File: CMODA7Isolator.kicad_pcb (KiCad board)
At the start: 2 copper layers, 78.7 x 82.6 mm, 49 parts, among them J1 Conn_01x24, J2 Conn_01x24, M1 Artix_7_35T_CMOD_A7, U1 TXB0108, U2 TXB0108, U3 TXB0108, U4 TXB0108, U5 TXB0108, U6 TXB0108, U7 LD1117S33TR_SOT223

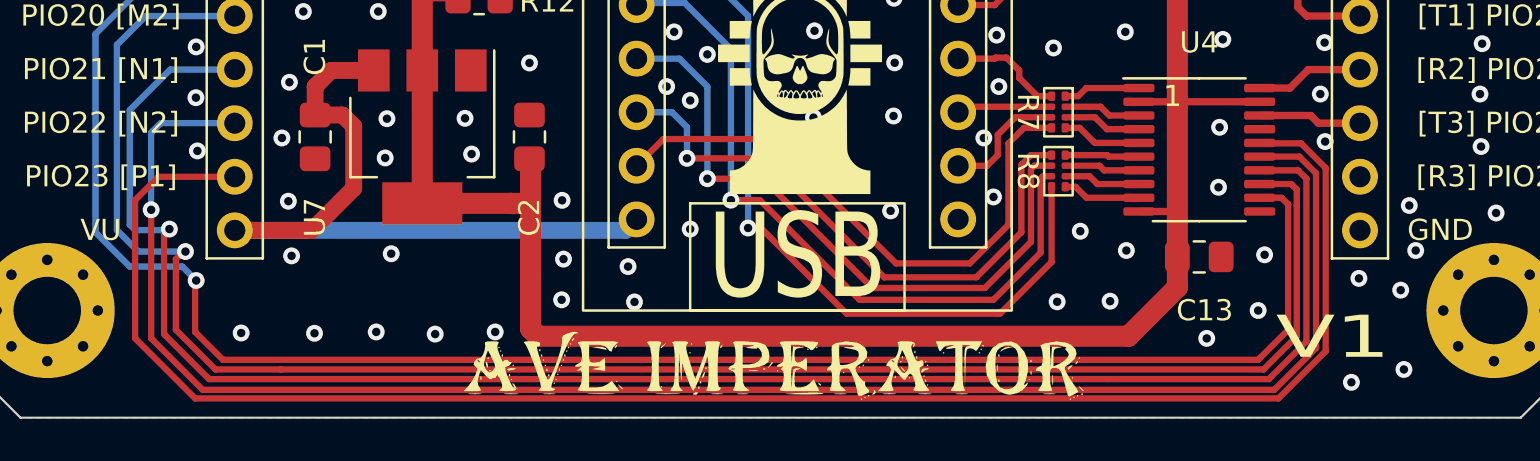
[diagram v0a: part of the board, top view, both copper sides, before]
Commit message: Fixed Issue #3
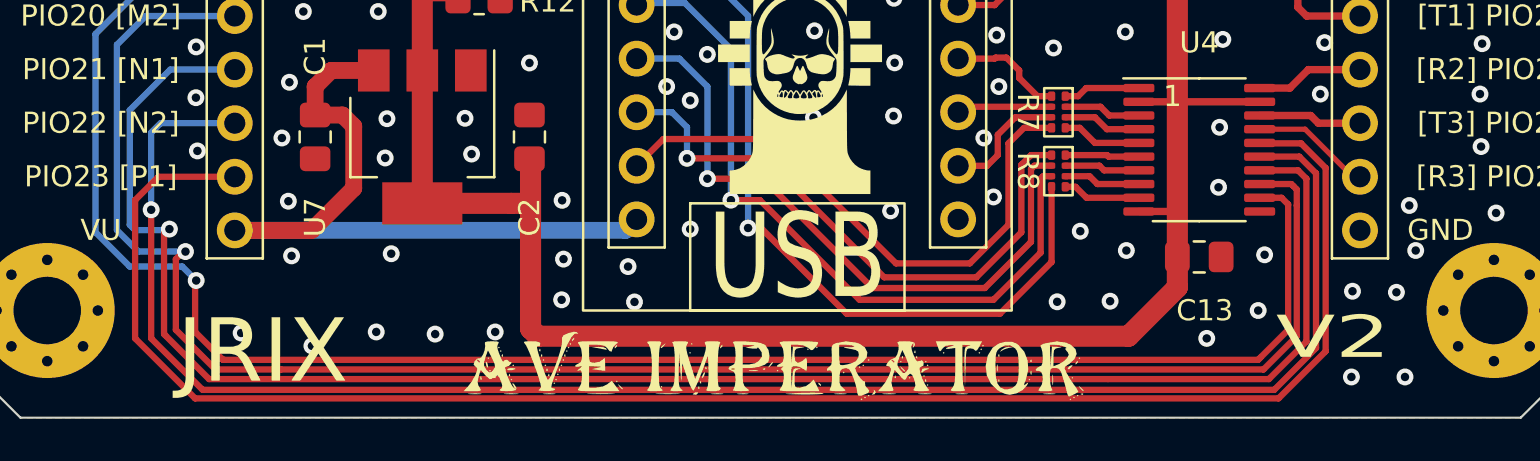
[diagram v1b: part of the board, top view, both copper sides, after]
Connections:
- U4 pad 17: /p024 -> /p026
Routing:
- net /p026: track 0.00 -> 5.69 mm
- net GND: vias 277 -> 276
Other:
- board text added: "JRIX"
- board text added: "V2"
- board text removed: "V1"
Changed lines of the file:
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@@
   (net 136 "/p39")
   (net 137 "/p40")
-  (net 138 "/p024")
+  (net 138 "Net-(D5-Pad2)")
   (net 139 "unconnected-(U6-Pad1)")
   (net 140 "unconnected-(U6-Pad3)")
@@
   (net 145 "unconnected-(U6-Pad18)")
   (net 146 "unconnected-(U6-Pad20)")
-  (net 147 "Net-(R12-Pad2)")
   (footprint "MountingHole:MountingHole_3.2mm_M3_Pad_Via" (layer "F.Cu")
     (at 53.34 39.37)
@@
       (net 2 "GND") (pinfunction "K") (pintype "passive"))
     (pad "2" smd roundrect (at 0.7875 0 293) (size 0.875 0.95) (layers "F.Cu" "F.Paste" "F.Mask") (roundrect_rratio 0.25)
-      (net 147 "Net-(R12-Pad2)") (pinfunction "A") (pintype "passive"))
+      (net 138 "Net-(D5-Pad2)") (pinfunction "A") (pintype "passive"))
     (model "${KICAD6_3DMODEL_DIR}/LED_SMD.3dshapes/LED_0603_1608Metric.wrl"
       (offset (xyz 0 0 0))
@@
       (net 3 "/3V3") (pintype "passive"))
     (pad "2" smd roundrect (at 1 0) (size 1.2 1.4) (layers "F.Cu" "F.Paste" "F.Mask") (roundrect_rratio 0.2083333333)
-      (net 147 "Net-(R12-Pad2)") (pintype "passive"))
+      (net 138 "Net-(D5-Pad2)") (pintype "passive"))
     (model "${KICAD6_3DMODEL_DIR}/Resistor_SMD.3dshapes/R_0805_2012Metric.wrl"
       (offset (xyz 0 0 0))
@@
       (net 26 "/p023") (pinfunction "B4") (pintype "bidirectional"))
     (pad "17" smd roundrect (at 2.8625 -0.975) (size 1.475 0.4) (layers "F.Cu" "F.Paste" "F.Mask") (roundrect_rratio 0.25)
-      (net 138 "/p024") (pinfunction "B3") (pintype "bidirectional"))
+      (net 49 "/p026") (pinfunction "B3") (pintype "bidirectional"))
     (pad "18" smd roundrect (at 2.8625 -1.625) (size 1.475 0.4) (layers "F.Cu" "F.Paste" "F.Mask") (roundrect_rratio 0.25)
       (net 48 "/p027") (pinfunction "B2") (pintype "bidirectional"))
@@
     (effects (font (size 1 1) (thickness 0.15)))
   )
-  (gr_text "V1" (at 114.3 113.03) (layer "F.SilkS")
+  (gr_text "V2" (at 114.3 113.03) (layer "F.SilkS")
     (effects (font (size 2 3) (thickness 0.5)))
   )
@@
     (effects (font (size 1 1) (thickness 0.15)))
   )
+  (gr_text "JRIX" (at 63.5508 113.6904) (layer "F.SilkS")
+    (effects (font (size 3 3) (thickness 0.4)))
+  )
   (gr_text "PIO19 [P3]" (at 55.88 95.25) (layer "F.SilkS")
     (effects (font (size 1 1) (thickness 0.15)))
@@
   (via (at 74.5744 112.776) (size 0.8) (drill 0.4) (layers "F.Cu" "B.Cu") (net 2))
   (via (at 64.9224 109.1692) (size 0.8) (drill 0.4) (layers "F.Cu" "B.Cu") (net 2))
-  (via (at 115.1636 115.1636) (size 0.8) (drill 0.4) (layers "F.Cu" "B.Cu") (net 2))
+  (via (at 115.1636 114.9096) (size 0.8) (drill 0.4) (layers "F.Cu" "B.Cu") (net 2))
   (via (at 93.458674 102.538985) (size 0.8) (drill 0.4) (layers "F.Cu" "B.Cu") (net 2))
   (via (at 93.6244 65.1764) (size 0.8) (drill 0.4) (layers "F.Cu" "B.Cu") (net 2))
@@
   (via (at 87.376 37.9476) (size 0.8) (drill 0.4) (layers "F.Cu" "B.Cu") (net 2))
   (via (at 80.2132 60.452) (size 0.8) (drill 0.4) (layers "F.Cu" "B.Cu") (net 2))
-  (via (at 113.917987 103.751487) (size 0.8) (drill 0.4) (layers "F.Cu" "B.Cu") (net 2))
   (via (at 63.754 78.5876) (size 0.8) (drill 0.4) (layers "F.Cu" "B.Cu") (net 2))
   (via (at 93.440454 91.123201) (size 0.8) (drill 0.4) (layers "F.Cu" "B.Cu") (net 2))
@@
   (via (at 97.7392 85.9028) (size 0.8) (drill 0.4) (layers "F.Cu" "B.Cu") (net 2))
   (via (at 73.4568 104.3432) (size 0.8) (drill 0.4) (layers "F.Cu" "B.Cu") (net 2))
-  (via (at 66.009829 112.839191) (size 0.8) (drill 0.4) (layers "F.Cu" "B.Cu") (net 2))
+  (via (at 65.8876 113.4364) (size 0.8) (drill 0.4) (layers "F.Cu" "B.Cu") (net 2))
   (via (at 89.027 91.313) (size 0.8) (drill 0.4) (layers "F.Cu" "B.Cu") (net 2))
   (via (at 50.209422 49.290135) (size 0.8) (drill 0.4) (layers "F.Cu" "B.Cu") (net 2))
@@
   (via (at 58.61089 40.806027) (size 0.8) (drill 0.4) (layers "F.Cu" "B.Cu") (net 2))
   (via (at 94.1324 40.5892) (size 0.8) (drill 0.4) (layers "F.Cu" "B.Cu") (net 2))
-  (via (at 117.6528 114.554) (size 0.8) (drill 0.4) (layers "F.Cu" "B.Cu") (net 2))
+  (via (at 117.7036 114.9096) (size 0.8) (drill 0.4) (layers "F.Cu" "B.Cu") (net 2))
   (via (at 68.9356 112.776) (size 0.8) (drill 0.4) (layers "F.Cu" "B.Cu") (net 2))
   (via (at 110.8456 63.3476) (size 0.8) (drill 0.4) (layers "F.Cu" "B.Cu") (net 2))
@@
   (via (at 97.8916 90.6272) (size 0.8) (drill 0.4) (layers "F.Cu" "B.Cu") (net 2))
   (via (at 50.114783 54.447968) (size 0.8) (drill 0.4) (layers "F.Cu" "B.Cu") (net 2))
-  (via (at 115.5192 110.236) (size 0.8) (drill 0.4) (layers "F.Cu" "B.Cu") (net 2))
+  (via (at 115.2144 110.8456) (size 0.8) (drill 0.4) (layers "F.Cu" "B.Cu") (net 2))
   (via (at 107.7976 47.3456) (size 0.8) (drill 0.4) (layers "F.Cu" "B.Cu") (net 2))
   (via (at 98.163883 52.776328) (size 0.8) (drill 0.4) (layers "F.Cu" "B.Cu") (net 2))
@@
   (via (at 93.493622 76.867361) (size 0.8) (drill 0.4) (layers "F.Cu" "B.Cu") (net 2))
   (via (at 50.256742 80.994248) (size 0.8) (drill 0.4) (layers "F.Cu" "B.Cu") (net 2))
-  (via (at 117.5004 110.7948) (size 0.8) (drill 0.4) (layers "F.Cu" "B.Cu") (net 2))
+  (via (at 117.2972 110.8964) (size 0.8) (drill 0.4) (layers "F.Cu" "B.Cu") (net 2))
   (via (at 98.3488 88.4936) (size 0.8) (drill 0.4) (layers "F.Cu" "B.Cu") (net 2))
   (via (at 84.0232 67.9196) (size 0.8) (drill 0.4) (layers "F.Cu" "B.Cu") (net 2))
@@
   (segment (start 113.2338 102.515) (end 113.5988 102.88) (width 0.35) (layer "F.Cu") (net 48))
   (segment (start 110.8125 102.515) (end 113.2338 102.515) (width 0.35) (layer "F.Cu") (net 48))
+  (segment (start 112.9694 103.165) (end 115.2244 105.42) (width 0.25) (layer "F.Cu") (net 49))
+  (segment (start 110.8125 103.165) (end 112.9694 103.165) (width 0.25) (layer "F.Cu") (net 49))
+  (segment (start 115.2244 105.42) (end 115.57 105.42) (width 0.25) (layer "F.Cu") (net 49))
   (segment (start 78.996 49.02) (end 81.28 49.02) (width 0.3) (layer "F.Cu") (net 50))
   (segment (start 78.232 54.102) (end 78.232 49.784) (width 0.3) (layer "F.Cu") (net 50))
@@
   (segment (start 100.076 73.66) (end 99.1616 72.7456) (width 0.3) (layer "F.Cu") (net 137))
   (segment (start 98.552 69.342) (end 98.5012 69.342) (width 0.3) (layer "F.Cu") (net 137))
-  (segment (start 74.8632 95.6564) (end 74.8632 86.354797) (width 0.25) (layer "F.Cu") (net 147))
-  (segment (start 74.8632 95.6564) (end 74.8632 96.9264) (width 0.3) (layer "F.Cu") (net 147))
-  (segment (start 74.8632 86.354797) (end 73.408901 84.900498) (width 0.25) (layer "F.Cu") (net 147))
-  (segment (start 74.8632 96.9264) (end 74.8124 96.9772) (width 0.3) (layer "F.Cu") (net 147))
+  (segment (start 74.8632 95.6564) (end 74.8632 86.354797) (width 0.25) (layer "F.Cu") (net 138))
+  (segment (start 74.8632 95.6564) (end 74.8632 96.9264) (width 0.3) (layer "F.Cu") (net 138))
+  (segment (start 74.8632 86.354797) (end 73.408901 84.900498) (width 0.25) (layer "F.Cu") (net 138))
+  (segment (start 74.8632 96.9264) (end 74.8124 96.9772) (width 0.3) (layer "F.Cu") (net 138))
   (zone (net 2) (net_name "GND") (layers F&B.Cu) (hatch edge 0.508)
     (connect_pads (clearance 0.508))
